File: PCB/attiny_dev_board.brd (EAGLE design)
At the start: 96.5 x 35.9 mm, 32 parts, among them J1 2-1571552-2

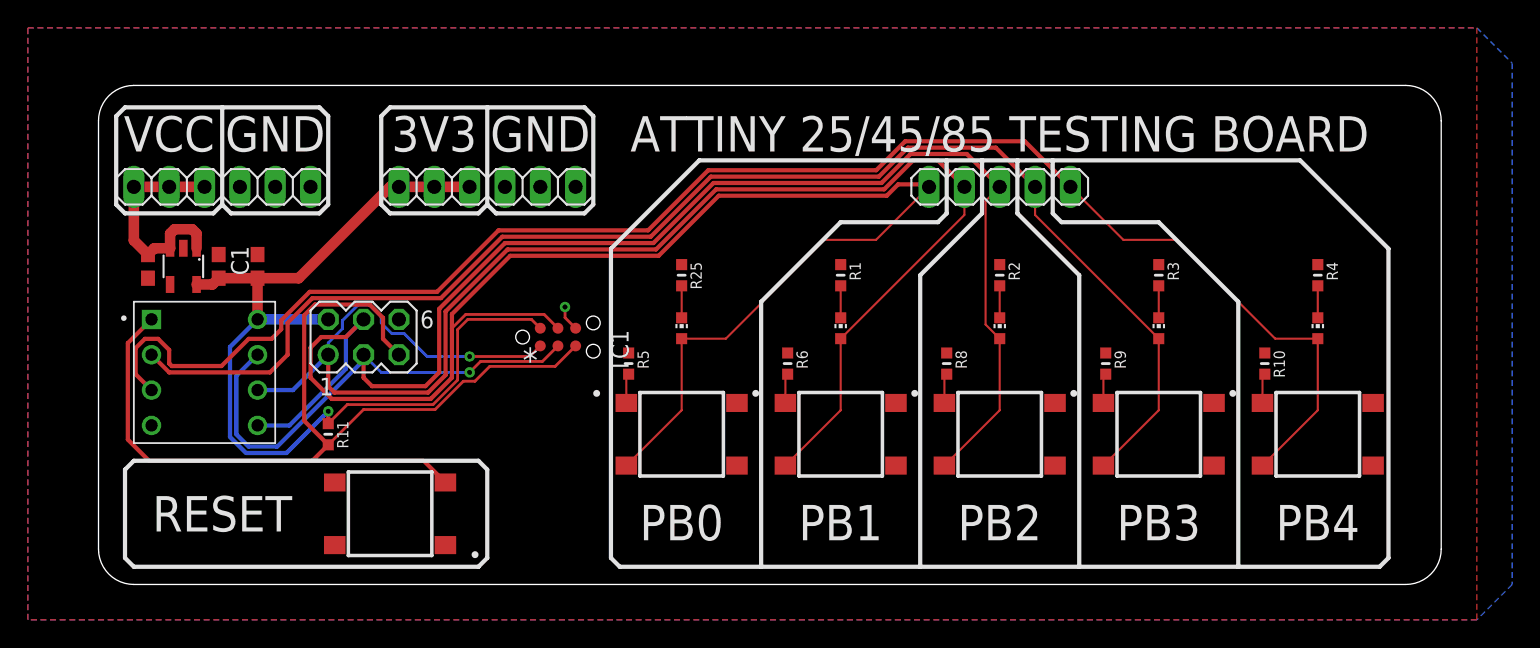
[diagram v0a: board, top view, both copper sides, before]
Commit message: Change to silkscreen
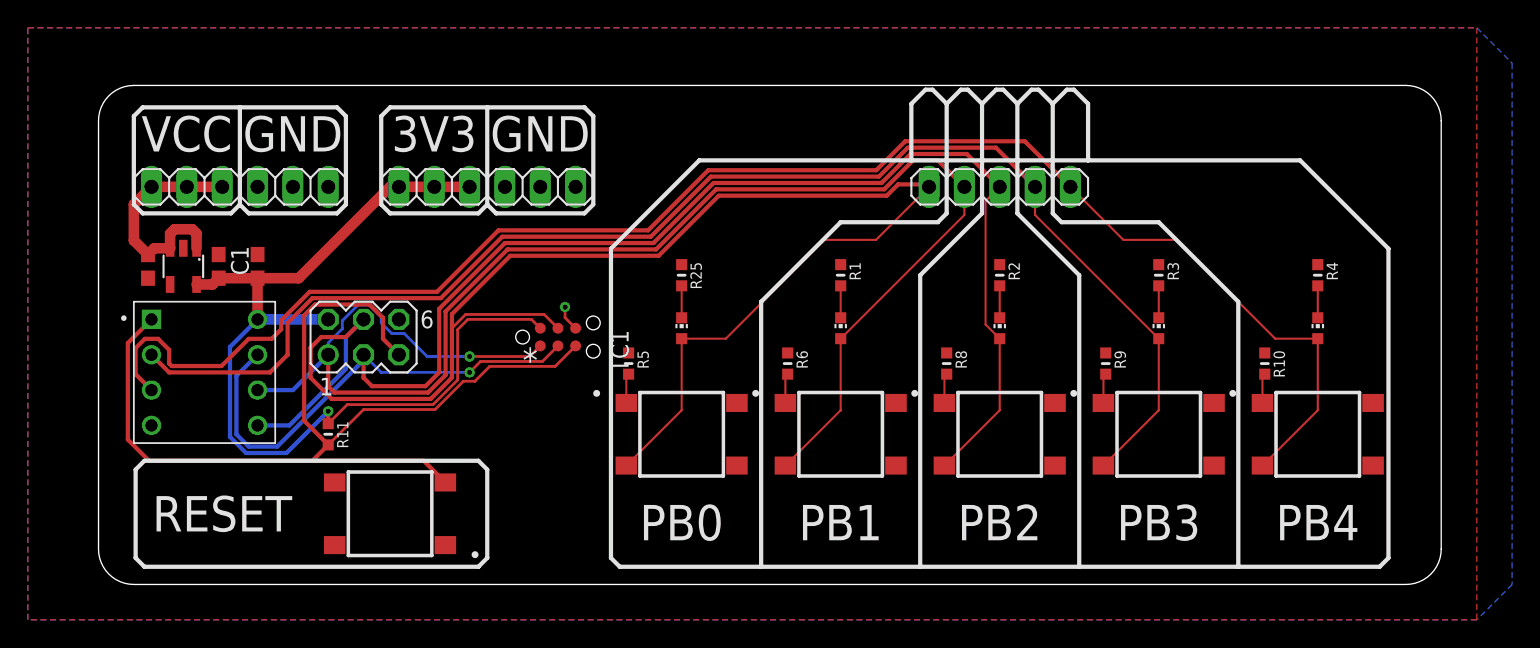
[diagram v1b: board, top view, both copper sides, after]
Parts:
- moved INPUT_POWER 1.27 mm to (10.2, 28.6)
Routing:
- net POWER_IN: track 16.4 -> 16.9 mm
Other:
- board text added: "ATTiny 25/45/85 development board"
- board text removed: "ATTINY 25/45/85 TESTING BOARD"
